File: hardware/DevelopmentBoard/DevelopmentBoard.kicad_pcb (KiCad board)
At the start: 2 copper layers, 93.7 x 66.3 mm, 16 parts, among them J1 12V connector, J2 Servo 1, J3 Servo 2, J4 JTAG, SW1 SW_Push, SW2 SW_Push, SW3 SW_Push, SW4 SW_Push

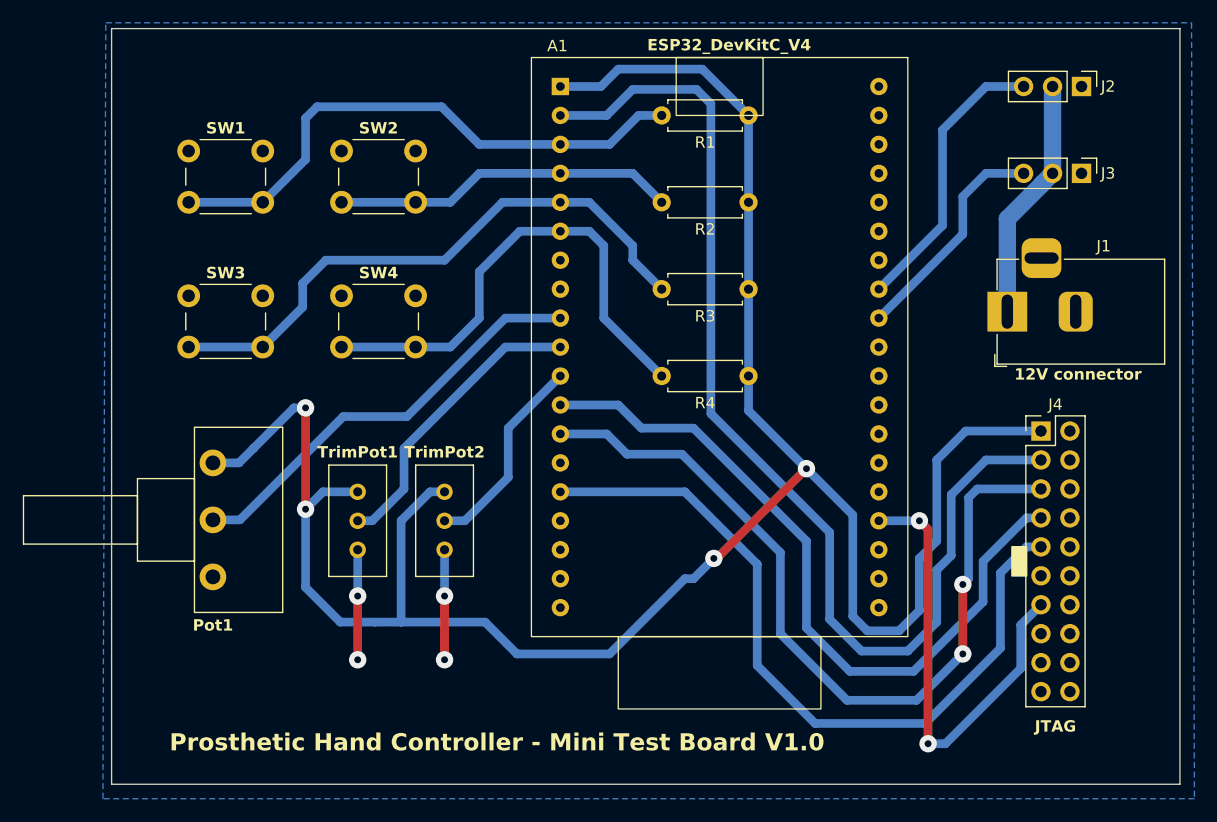
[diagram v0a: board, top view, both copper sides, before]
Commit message: Update ESP32 footprint
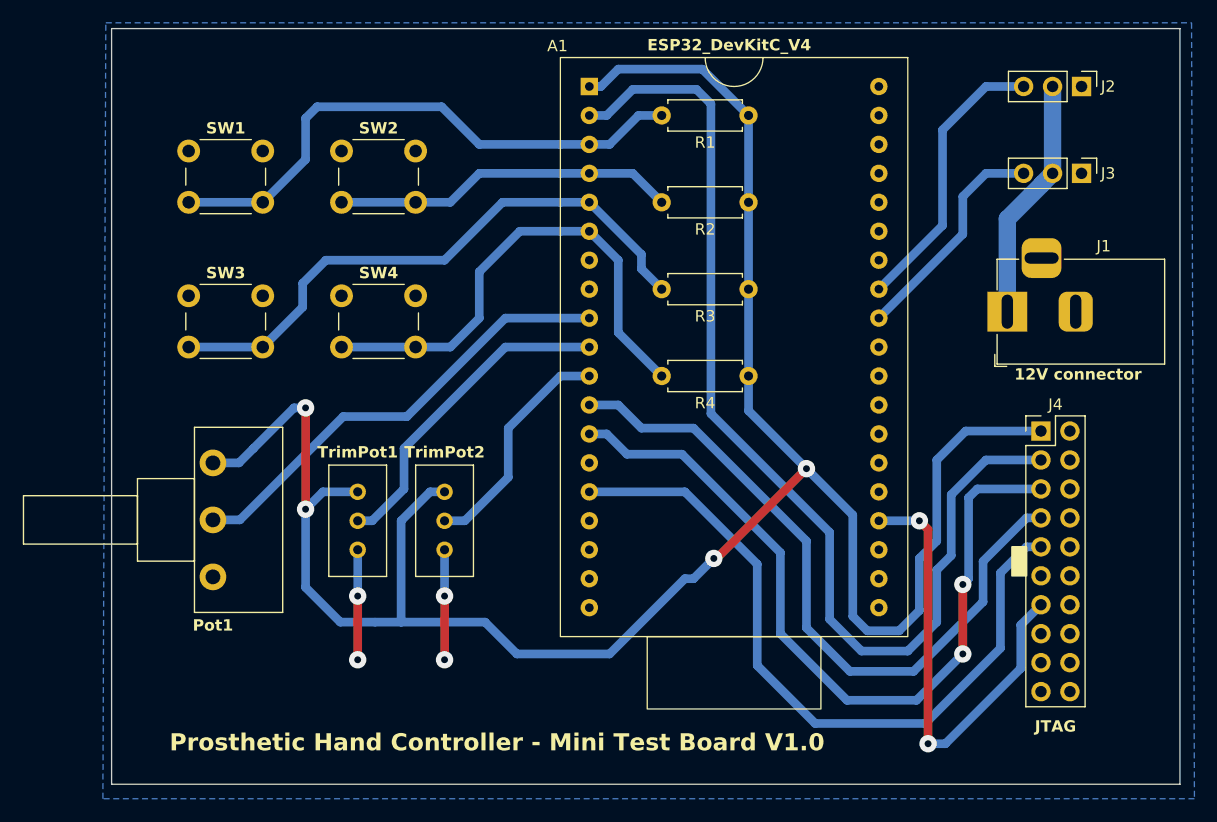
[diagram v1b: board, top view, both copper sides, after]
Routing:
- net VCC: track 196.0 -> 193.1 mm
- net Net-(A1-13): track 66.1 -> 63.5 mm
- net Net-(A1-27): track 17.9 -> 20.5 mm
- net Net-(A1-26): track 26.2 -> 28.7 mm
- net Net-(A1-25): track 37.8 -> 40.4 mm
- net Net-(A1-14): track 64.0 -> 61.4 mm
- net Net-(A1-12): track 70.7 -> 68.2 mm
- net Net-(A1-EN): track 96.7 -> 94.1 mm
